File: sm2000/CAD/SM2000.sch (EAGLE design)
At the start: 361 parts, among them CN1 HDR100-3, CN10 ST-3509, CN11 HDR100-3, CN2 JS-MU3-002, CN3 DS-0518, CN5 ST-3509, CN8 ST-3509, J1 JMP-2PIN, J2 JMP-2PIN, J3 JMP-2PIN, J4 CONN-BOOM-XH-2A, P10 TPAD50, P11 TPAD50, P12 TPAD50, P13 TPAD50, P14 TPAD50, P16 TPAD50, P18 TPAD50, P19 TPAD50, P20 TPAD50, P21 TPAD50, P3 TPAD50, P4 TPAD50, P5 TPAD50, P6 TPAD50, P7 TPAD50, P8 TPAD50, P9 TPAD50, Q1 MMBT3904, Q10 MMBT3904, Q11 STR2P3LLH6, Q12 BRF92, Q13 BFQ19, Q14 RD01MUS2, Q15 MMBT3904, Q17 MMBT3904, Q18 MMBT3904, Q2 MMBT3904, Q3 MMBT3904, Q4 MMBT3904, Q5 MMBT3904, Q6 MMBT3904, Q7 BC548, Q8 BC549, Q9 STR2P3LLH6, SW1 SW-LC2259, SW2 TS-026, SW3 SW-LC2259EENP, SW4 TS-026, SW5 TS-02B, U1 STM32F405VGT6, U10 DNL, U11 L78MXX, U12 PGA-103+, U13 ADE-1, U14 SI570, U15 SI5351A, U2 L78MXX, U3 STMPS2141, U4 EMIF02-USB03F2, U5 L78MXX, U6 LD3985M33R, U7 SA612A, U8 LM386M-1, U9 LMV341, X1 BU-SMA-H, X2 BU-SMA-H

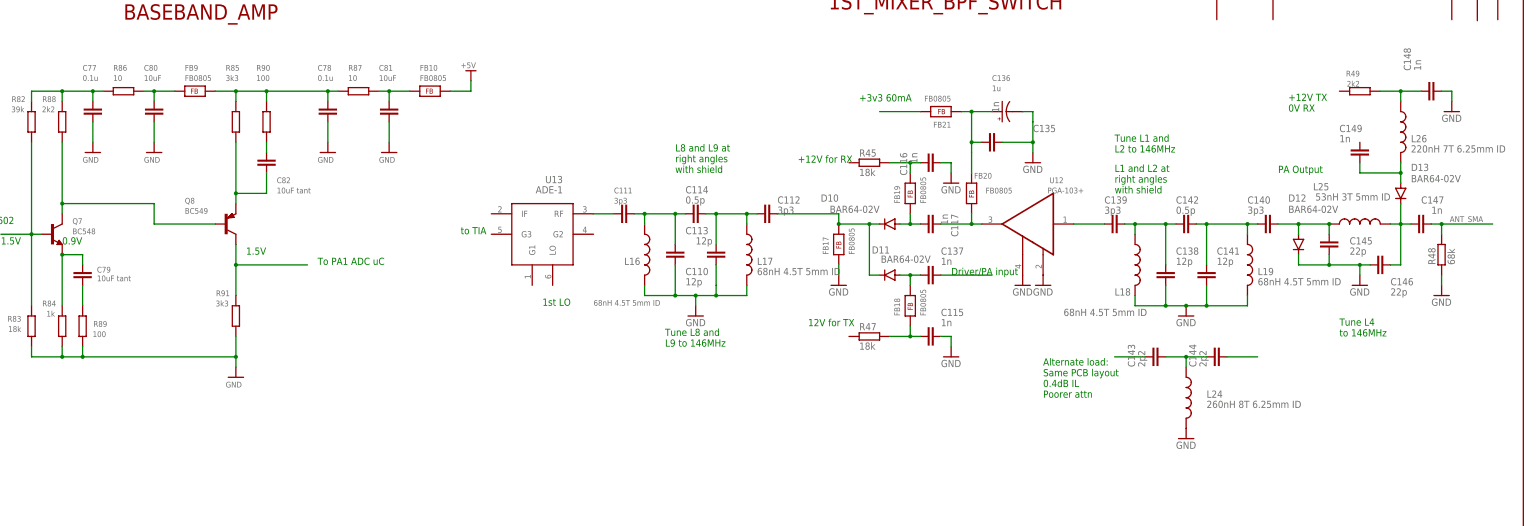
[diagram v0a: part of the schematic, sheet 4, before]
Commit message: 
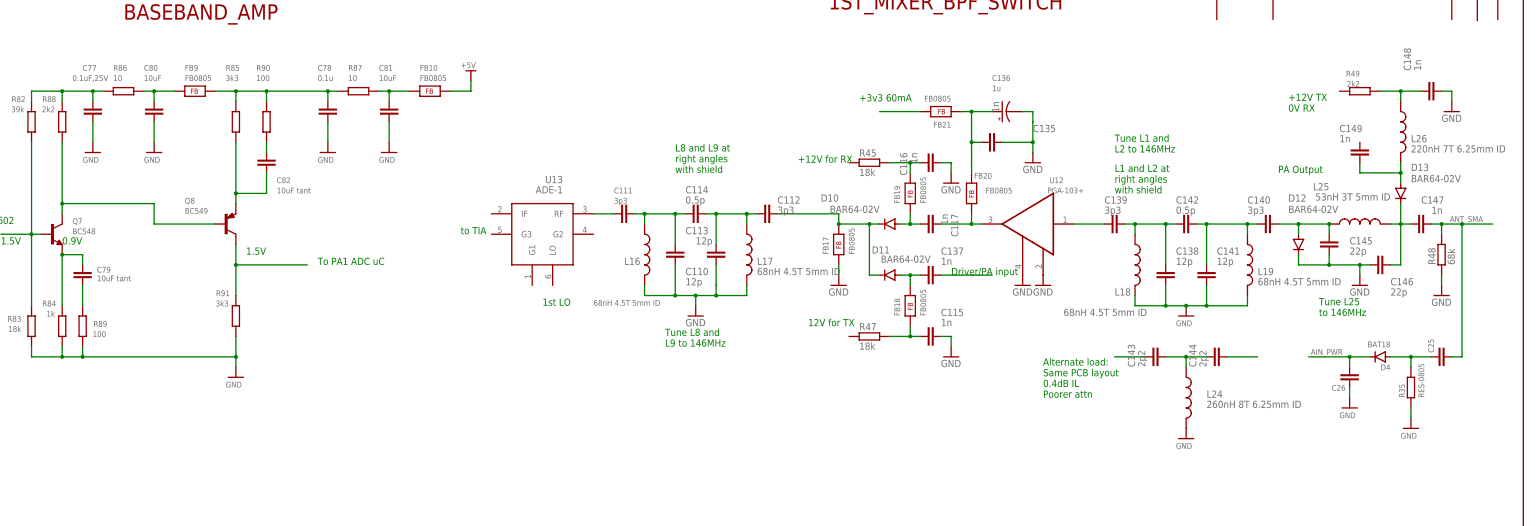
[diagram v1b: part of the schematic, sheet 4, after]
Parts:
- added C25, C26: (no value), _RoweTel:CAP-0805
- added D4: BAT18, _RoweTel:BAT18
- added R35: RES-0805, _RoweTel:RES-0805
- C77: value 0.1u -> 0.1uF,25V
- Q7: device transistor:-NPN-SOT23-EBC -> _RoweTel:MMBT3904
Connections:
- new net AIN_PWR: C26.2, D4.K
- new net N$57: C25.1, D4.A, R35.2
- net ANT_SMA: now also C25.2
- net GND: now also C26.1, R35.1
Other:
- note added: "Tune L25 to 146MHz"
- note removed: "Tune L4 to 146MHz"
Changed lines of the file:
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@@
 <layer number="101" name="Gehäuse" color="13" fill="1" visible="no" active="yes"/>
 <layer number="102" name="Mittellin" color="7" fill="1" visible="no" active="yes"/>
+<layer number="103" name="fp3" color="7" fill="1" visible="no" active="yes"/>
+<layer number="104" name="Name" color="7" fill="1" visible="no" active="yes"/>
 <layer number="105" name="Beschreib" color="9" fill="1" visible="no" active="no"/>
 <layer number="106" name="BGA-Top" color="4" fill="1" visible="no" active="no"/>
 <layer number="107" name="BD-Top" color="5" fill="1" visible="no" active="no"/>
+<layer number="108" name="fp8" color="7" fill="1" visible="no" active="yes"/>
+<layer number="109" name="fp9" color="7" fill="1" visible="no" active="yes"/>
+<layer number="110" name="fp0" color="7" fill="1" visible="no" active="yes"/>
+<layer number="111" name="KASTMAAT1" color="7" fill="1" visible="no" active="yes"/>
+<layer number="112" name="KASTMAAT2" color="7" fill="1" visible="no" active="yes"/>
+<layer number="113" name="FRNTTEKEN" color="7" fill="1" visible="no" active="yes"/>
+<layer number="114" name="FRNTMAAT1" color="7" fill="1" visible="no" active="yes"/>
+<layer number="115" name="FRNTMAAT2" color="7" fill="1" visible="no" active="yes"/>
+<layer number="116" name="Patch_BOT" color="7" fill="1" visible="no" active="yes"/>
+<layer number="117" name="BACKMAAT1" color="7" fill="1" visible="no" active="yes"/>
+<layer number="118" name="BACKMAAT2" color="7" fill="1" visible="no" active="yes"/>
+<layer number="119" name="KAP_TEKEN" color="7" fill="1" visible="no" active="yes"/>
+<layer number="120" name="KAP_MAAT1" color="7" fill="1" visible="no" active="yes"/>
+<layer number="121" name="tTestdril" color="7" fill="1" visible="no" active="yes"/>
+<layer number="122" name="bTestdril" color="7" fill="1" visible="no" active="yes"/>
+<layer number="123" name="tTestmark" color="7" fill="1" visible="no" active="yes"/>
+<layer number="124" name="bTestmark" color="7" fill="1" visible="no" active="yes"/>
+<layer number="125" name="BIFRNTTEK" color="7" fill="1" visible="no" active="yes"/>
+<layer number="126" name="BIFRNTMAT" color="7" fill="1" visible="no" active="yes"/>
+<layer number="130" name="SMDSTROOK" color="7" fill="1" visible="no" active="yes"/>
+<layer number="131" name="tAdjust" color="7" fill="1" visible="no" active="yes"/>
+<layer number="132" name="bAdjust" color="7" fill="1" visible="no" active="yes"/>
+<layer number="144" name="Drill_legend" color="7" fill="1" visible="no" active="yes"/>
+<layer number="151" name="HeatSink" color="7" fill="1" visible="no" active="yes"/>
+<layer number="199" name="Contour" color="7" fill="1" visible="no" active="yes"/>
 <layer number="200" name="200bmp" color="1" fill="10" visible="no" active="no"/>
+<layer number="201" name="Construction" color="7" fill="1" visible="no" active="yes"/>
+<layer number="202" name="TDIM" color="7" fill="1" visible="no" active="yes"/>
+<layer number="203" name="BDIM" color="7" fill="1" visible="no" active="yes"/>
+<layer number="204" name="BRD-DIM" color="7" fill="1" visible="no" active="yes"/>
+<layer number="205" name="SECTION-OTL" color="7" fill="1" visible="no" active="yes"/>
+<layer number="206" name="206bmp" color="7" fill="1" visible="no" active="yes"/>
+<layer number="207" name="207bmp" color="7" fill="1" visible="no" active="yes"/>
+<layer number="208" name="208bmp" color="7" fill="1" visible="no" active="yes"/>
+<layer number="209" name="209bmp" color="7" fill="1" visible="no" active="yes"/>
+<layer number="210" name="210bmp" color="7" fill="1" visible="no" active="yes"/>
+<layer number="216" name="BottomExtra" color="7" fill="1" visible="no" active="yes"/>
 <layer number="250" name="Descript" color="3" fill="1" visible="no" active="no"/>
 <layer number="251" name="SMDround" color="12" fill="11" visible="no" active="no"/>
+<layer number="254" name="OrgLBR" color="7" fill="1" visible="no" active="yes"/>
+<layer number="255" name="Accent" color="7" fill="1" visible="no" active="yes"/>
 </layers>
 <schematic xreflabel="%F%N/%S.%C%R" xrefpart="/%S.%C%R">
@@
 <part name="V161" library="A-SUPPLY2" deviceset="GND" device=""/>
 <part name="V162" library="A-SUPPLY2" deviceset="GND" device=""/>
-<part name="Q7" library="transistor" deviceset="*-NPN-" device="SOT23-EBC" value="BC548"/>
+<part name="Q7" library="_RoweTel" deviceset="MMBT3904" device="" value="BC548"/>
 <part name="R82" library="_RoweTel" deviceset="RES-0805" device="" value="39k"/>
 <part name="R83" library="_RoweTel" deviceset="RES-0805" device="" value="18k"/>
@@
 <part name="R85" library="_RoweTel" deviceset="RES-0805" device="" value="3k3"/>
 <part name="R86" library="_RoweTel" deviceset="RES-0805" device="" value="10"/>
-<part name="C77" library="_RoweTel" deviceset="CAP-0805" device="" value="0.1u"/>
+<part name="C77" library="_RoweTel" deviceset="CAP-0805" device="" value="0.1uF,25V"/>
 <part name="C78" library="_RoweTel" deviceset="CAP-0805" device="" value="0.1u"/>
 <part name="R87" library="_RoweTel" deviceset="RES-0805" device="" value="10"/>
@@
 <part name="U14" library="_RoweTel" deviceset="SI570" device=""/>
 <part name="U$7" library="A-SUPPLY2" deviceset="+3.3V" device=""/>
+<part name="D4" library="_RoweTel" deviceset="BAT18" device=""/>
+<part name="R35" library="_RoweTel" deviceset="RES-0805" device=""/>
+<part name="C25" library="_RoweTel" deviceset="CAP-0805" device=""/>
+<part name="C26" library="_RoweTel" deviceset="CAP-0805" device=""/>
+<part name="GND18" library="supply1" deviceset="GND" device=""/>
+<part name="GND19" library="supply1" deviceset="GND" device=""/>
 </parts>
 <sheets>
@@
 right angles
 with shield</text>
-<text x="386.08" y="185.42" size="1.778" layer="91">Tune L4
+<text x="381" y="190.5" size="1.778" layer="91">Tune L25
 to 146MHz</text>
 <text x="259.08" y="266.7" size="3.81" layer="94" ratio="10">1ST_MIXER_BPF_SWITCH</text>
@@
 <instance part="C77" gate="G$1" x="76.2" y="241.3" smashed="yes">
 <attribute name="NAME" x="73.66" y="251.46" size="1.4224" layer="95"/>
-<attribute name="VALUE" x="73.66" y="248.92" size="1.4224" layer="96"/>
+<attribute name="VALUE" x="71.12" y="248.92" size="1.4224" layer="96"/>
 </instance>
 <instance part="C78" gate="G$1" x="134.62" y="241.3" smashed="yes">
@@
 </instance>
 <instance part="GND45" gate="1" x="347.98" y="190.5" smashed="yes">
-<attribute name="VALUE" x="345.44" y="187.96" size="1.778" layer="96"/>
+<attribute name="VALUE" x="345.44" y="187.96" size="1.4224" layer="96"/>
 </instance>
 <instance part="L24" gate="G$1" x="347.98" y="170.18" smashed="yes">
@@
 </instance>
 <instance part="GND46" gate="1" x="347.98" y="160.02" smashed="yes">
-<attribute name="VALUE" x="345.44" y="157.48" size="1.778" layer="96"/>
+<attribute name="VALUE" x="345.44" y="157.48" size="1.4224" layer="96"/>
 </instance>
 <instance part="D12" gate="G$1" x="375.92" y="208.28" smashed="yes" rot="R270">
@@
 <attribute name="VALUE" x="162.56" y="122.555" size="1.4224" layer="96" ratio="9"/>
 </instance>
+<instance part="D4" gate="G$1" x="396.24" y="180.34" rot="R180"/>
+<instance part="R35" gate="G$1" x="403.86" y="172.72" rot="R90"/>
+<instance part="C25" gate="G$1" x="411.48" y="180.34" rot="R90"/>
+<instance part="C26" gate="G$1" x="388.62" y="175.26" rot="R180"/>
+<instance part="GND18" gate="1" x="388.62" y="167.64" smashed="yes">
+<attribute name="VALUE" x="386.08" y="165.1" size="1.4224" layer="96"/>
+</instance>
+<instance part="GND19" gate="1" x="403.86" y="162.56" smashed="yes">
+<attribute name="VALUE" x="401.32" y="160.02" size="1.4224" layer="96"/>
+</instance>
 </instances>
 <busses>
@@
 <junction x="391.16" y="203.2"/>
 </segment>
+<segment>
+<pinref part="C26" gate="G$1" pin="1"/>
+<wire x1="388.62" y1="172.72" x2="388.62" y2="170.18" width="0.1524" layer="91"/>
+<pinref part="GND18" gate="1" pin="GND"/>
+</segment>
+<segment>
+<pinref part="R35" gate="G$1" pin="1"/>
+<wire x1="403.86" y1="167.64" x2="403.86" y2="165.1" width="0.1524" layer="91"/>
+<pinref part="GND19" gate="1" pin="GND"/>
+</segment>
 </net>
 <net name="N$103" class="0">
@@
 <wire x1="408.94" y1="213.36" x2="411.48" y2="213.36" width="0.1524" layer="91"/>
 <pinref part="R48" gate="G$1" pin="2"/>
-<wire x1="411.48" y1="213.36" x2="424.18" y2="213.36" width="0.1524" layer="91"/>
+<wire x1="411.48" y1="213.36" x2="416.56" y2="213.36" width="0.1524" layer="91"/>
+<wire x1="416.56" y1="213.36" x2="424.18" y2="213.36" width="0.1524" layer="91"/>
 <wire x1="411.48" y1="210.82" x2="411.48" y2="213.36" width="0.1524" layer="91"/>
 <junction x="411.48" y="213.36"/>
 <label x="413.512" y="213.868" size="1.4224" layer="95" ratio="10"/>
+<wire x1="416.56" y1="213.36" x2="416.56" y2="180.34" width="0.1524" layer="91"/>
+<pinref part="C25" gate="G$1" pin="2"/>
+<wire x1="416.56" y1="180.34" x2="414.02" y2="180.34" width="0.1524" layer="91"/>
+<junction x="416.56" y="213.36"/>
 </segment>
 </net>
@@
 </segment>
 </net>
+<net name="N$57" class="0">
+<segment>
+<pinref part="C25" gate="G$1" pin="1"/>
+<pinref part="D4" gate="G$1" pin="A"/>
+<wire x1="408.94" y1="180.34" x2="403.86" y2="180.34" width="0.1524" layer="91"/>
+<pinref part="R35" gate="G$1" pin="2"/>
+<wire x1="403.86" y1="180.34" x2="398.78" y2="180.34" width="0.1524" layer="91"/>
+<wire x1="403.86" y1="177.8" x2="403.86" y2="180.34" width="0.1524" layer="91"/>
+<junction x="403.86" y="180.34"/>
+</segment>
+</net>
+<net name="AIN_PWR" class="0">
+<segment>
+<pinref part="D4" gate="G$1" pin="K"/>
+<pinref part="C26" gate="G$1" pin="2"/>
+<wire x1="393.7" y1="180.34" x2="388.62" y2="180.34" width="0.1524" layer="91"/>
+<wire x1="388.62" y1="180.34" x2="388.62" y2="177.8" width="0.1524" layer="91"/>
+<wire x1="388.62" y1="180.34" x2="378.46" y2="180.34" width="0.1524" layer="91"/>
+<junction x="388.62" y="180.34"/>
+<label x="378.968" y="180.848" size="1.4224" layer="95" ratio="10"/>
+</segment>
+</net>

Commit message: Intermediate update: Fix resistor tolerances fix cap working voltages Fix some library items for no name & no value email Schematic Updates 01/01/2016 item 1. email Commits to SVN 01/02/2016 items 1, i,ii,iii,iv, 2,3,4 RGB
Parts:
- removed C36, C47: 1uF,16V, _RoweTel:CAP-0805
- removed C38: 10nF,25V, _RoweTel:CAP-0805
- removed C41, C45: 100nF,25V, _RoweTel:CAP-0805
- removed LED6: DNL, _RoweTel:SML-LX0603SRW
- removed R23: 0 Ohm, _RoweTel:RES-0805
- removed R9: DNL, _RoweTel:RES-0805
- removed U6: LD3985M33R, _RoweTel:LD3985
- removed X1, X2: BU-SMA-H, _RoweTel:BU-SMA-H
- C100, C93: value 33p -> 33pF,50V
- C110: value 12p -> 12pF.50V
- C111, C112, C139, C140: value 3p3 -> 3.3pF,50V
- C113, C138, C141: value 12p -> 12pF,50V
- C114, C142: value 0.5p -> 0.5pF,50V
- C115, C116, C117, C130, C133, C134, C135, C137, C147, C148, C149, C88, C90, C96, C98: value 1n -> 1nF,25V
- C118, C121, C124, C125, C126, C131, C78: value 0.1u -> 0.1uF,25V
- C120: value 39pF -> 39pF,50V
- C122, C89: value 5p6 -> 5.6pF,50V
- C127: value 27pF -> 27pF,50V
- C128, C132: value 150pF -> 150pF,50V
- C129, C91, C92, C97: value 0.1u -> 0.1uF.25V
- C136: value 1u -> 1uF,25V
- C143, C144: value 2p2 -> 2.2pF,50V
- C145, C94: value 22p -> 22pF,50V
- C146: value 22p -> 22pF,25V
- C25: value (none) -> 1pF,50V
- C26: value (none) -> 1nF,25V
- C28: value 100nF -> 100nF,25V
- C87: value 22pF -> 22pF,50V
- C95: value 1n DNL -> 1nF,25V
- C99: value 47p -> 47pF,50V
- L14, L15: value 57nH air core 4T 2mm ID -> 57nH
- L16, L17, L18, L19: value 68nH 4.5T 5mm ID -> 68nH
- L24: value 260nH 8T 6.25mm ID -> 260nH
- L26: value 220nH 7T 6.25mm ID -> 220nH
- Q7: value BC548 -> MMBT3904
- Q8: value BC549 -> MMBT3906
- R101, R104, R115, R92: value 150 -> 150,1%
- R102, R103, R109, R113, R84, R94: value 1k -> 1K,1%
- R105, R106, R107: value 0R -> 0 Ohm
- R108, R60, R93: value 3k -> 3K,1%
- R110, R70, R80, R86, R87, R96, R97: value 10 -> 10,1%
- R111: value 33k -> 33K,1%
- R112: value 15k -> 15K,1%
- R114: value 50 -> 50,1%
- R35: value RES-0805 -> 330,1%
- R45, R47, R83: value 18k -> 18K,1%
- R48: value 68k -> 68K,1%
- R49, R88: value 2k2 -> 2.2K,1%
- R55: value 10k -> 10K,1%
- R59, R72: value 330 -> 330,1%
- R63, R73: value 680 -> 680,1%
- R64, R74: value 10K -> 10K,1%
- R65, R68, R75, R78: value 2.2K -> 2.2K,1%
- R66, R76: value 180 -> 180,1%
- R67, R77: value 15 -> 15,1%
- R69, R79: value 470 -> 470,1%
- R71, R81: value 47 -> 47,1%
- R82: value 39k -> 39K,1%
- R85, R91: value 3k3 -> 3.3K,1%
- R89, R90: value 100 -> 100,1%
- R95: value 50 -> 49.4,1%
- R98: value 47 DNL -> 47,1%, DNL
- R99: value 4k7 -> 4.7K,1%
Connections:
- net N$38 renamed DRIVER/PA_INPUT
- removed net N$100: C71.2, C75.1, X1.1
- removed net N$37 (its old number): C38.1, U6.BYBASS
- removed net N$40: Q11.D, R80.1
- removed net N$52: LED6.A, R9.1
- removed net N$56: L20.1
- removed net N$79: L11.2, L13.2, R97.1
- removed net N$90: C69.1, C76.2, X2.1
- new net N$19: L13.1, R97.1
- new net PA_OUTPUT: C149.2
- new net RX+12V: Q9.D, R70.2
- new net TIAIN: C71.2, C75.1, U13.G3
- new net TIAOUT: C69.1, C76.2, L20.1
- new net TX+12V: L11.2, Q11.D, R47.1, R49.2, R80.1
- net +12V: no longer Q11.S, Q9.S, R17.2, R33.2
- net +12V_RX: now also R45.1; no longer Q9.D, R70.2
- net +3.3V: no longer C36.1, C41.1, R23.1, R9.2, U6.VOUT
- net +5V: no longer C45.1, C47.1, U6.INH, U6.VIN
- net +9V: now also L13.2; no longer L13.1
- net +VIN: now also Q11.S, Q9.S, R17.2, R33.2
- net GND: no longer C36.2, C38.2, C41.2, C45.2, C47.2, LED6.C, U6.GND, X1.2, X2.2
- net VDD: no longer R23.2
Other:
- note added: "ADC3"
- note added: "L10 6T 6.25mm"
- note added: "L12 3T 6.25mm"
- note added: "L14 57nH, Air Core, 4T, 2mm ID"
- note added: "L15 57nH, Air Core, 4T, 2mm ID"
- note added: "L16 68nH,4.5T 5mm ID"
- note added: "L17 68nH,4.5T 5mm ID"
- note added: "L18 68nH,4.5T 5mm ID"
- note added: "L19 68nH,4.5T 5mm ID"
- note added: "L24 260nH 8T 6.25mm ID"
- note added: "L25 53nH,3T 5mm ID"
- note added: "L26 220nH,7T 6.25mm ID"
- note added: "L9 3T 6.25mm"
- note added: "TERMINATION INSENSiTIVE AMPLIFIEER"
- note removed: "+12V TX 0V RX"
- note removed: "+12V for RX"
- note removed: "1K,1%"
- note removed: "5.0V -> 3.3V PS"
- note removed: "6T 6.25mm"
- note removed: "Driver/PA input"
- note removed: "From TIA"
- note removed: "PA Output"
- note removed: "SML-LX0603SRW-TR"
- note removed: "TERMINATION INSENSATIVE AMPLIFIEER"
- moved on the sheet: C100, C110, C111, C112, C113, C114, C138, C139, C140, C141, C149, C77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

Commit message: Update schematic. Moved new component footprints onto PCB Matched schematic to emailchange lists. reorganized circuitry blocks on pages. RGB
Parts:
- added C27: 1nF,25V, _RoweTel:CAP-0805
- added J10, J11, J12, J5, J6, J7, J8, J9: JMPR-2X2, _RoweTel:JMPR-2X2
- added SH4, SH5: SHUNT, _RoweTel:SHUNT
- C119, C80, C81: value 10uF -> 10uF,25V,EL; device _RoweTel:CAP-0805 -> _RoweTel:CAP-10UF-WJ5
- C79, C82: value 10uF tant -> 10uF,25V,EL; device _RoweTel:CAP-0805 -> _RoweTel:CAP-10UF-WJ5
- R114: value 50,1% -> 49.9,1%
- R95: value 49.4,1% -> 49.9,1%
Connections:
- net +12V_RX_ENB renamed +12VRXENB
- removed net N$127: C111.2, U13.RF
- new net N$40: C126.2, J6.1
- new net N$52: C100.1, J9.1, L14.2
- new net N$56: C111.2, J12.2
- new net N$58: J12.1, U13.RF
- new net N$59: C27.2, J10.1
- new net N$61: C27.1, U12.1N
- new net N$63: J8.1
- new net N$79: C112.1, J11.1
- new net TIA_OUT: C69.1, C76.2, J5.1, L20.1
- net ANT_SMA: now also J9.2; no longer C100.1, L14.2
- net BBAMP: now also J7.1
- net GND: now also J10.3, J10.4, J11.3, J11.4, J12.3, J12.4, J5.3, J5.4, J6.3, J6.4, J7.3, J7.4, J8.3, J8.4, J9.3, J9.4
- net N$104: now also J7.2
- net N$11: now also J10.2; no longer U12.1N
- net N$112: now also J8.2
- net N$135: now also J11.2; no longer C112.1
- net N$49: now also J6.2; no longer C126.2
- net TIAOUT: now also J5.2; no longer C69.1, C76.2, L20.1
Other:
- note added: "+12V RX PWR"
- note added: "+12V TX PWR"
- note added: "VDD -> AVDD"
- note removed: "VDD -> AVDD POWER SOURCE"
- moved on the sheet: C1, C100, C110, C111, C112, C113, C114, C115, C116, C117, C126, C135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

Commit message: Implemented changes from D. Rowes email: Comments #1 RGB
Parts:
- removed C64: 22uF,25V, _RoweTel:CAP-0805
- removed C66: 100nF,25V, _RoweTel:CAP-0805
- removed U5: L78MXX, _RoweTel:L78MXX
- added C101: 10nF,25V, _RoweTel:CAP-0805
- added C103, C164: 100nF,25V, _RoweTel:CAP-0805
- added C107: 100nF,25V, AA-ipc-7351-capacitor:CAPACITOR_0402
- added C108: 20pF,50V, AA-ipc-7351-capacitor:CAPACITOR_0402
- added C109: 8.2nF,25V, ipc-7351-capacitor:CAPACITOR_0603
- added C150, C179: 22uF,25V, _RoweTel:CAP-1210
- added C166: 470nF,25V, ipc-7351-capacitor:CAPACITOR_0603
- added C167: 22uF,25V,1210, AA-ipc-7351-capacitor:CAPACITOR_1210
- added C29, C31: CAP-10UF-WJ5, _RoweTel:CAP-10UF-WJ5
- added C36: 1nF,25V, _RoweTel:CAP-0805
- added J13: JMPR-2X2, _RoweTel:JMPR-2X2
- added L1: 4.2uH, _RoweTel:SRR5028
- added R127: 124.0K,1%, AA-ipc-7351-resistor:RESISTOR_0402
- added R128: 22.1K,1%, AA-ipc-7351-resistor:RESISTOR_0402
- added R129: 10K,1%, AA-ipc-7351-resistor:RESISTOR_0402
- added U17: TPS54329E, _RoweTel:TPS54329E
- added U6: LD3985M33R, _RoweTel:LD3985
- C1: value .33uF,25V -> 100nF,25V
- C5, C7: value .33uF,25V -> CAP-10UF-WJ5; device _RoweTel:CAP-0805 -> _RoweTel:CAP-10UF-WJ5
- C65: value 1uF,16V -> 1uF,25V
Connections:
- removed net N$63: J8.1
- new net N$127: C101.1, U6.BYBASS
- new net N$169: C107.1, U17.VBST
- new net N$170: C108.2, R127.2, R128.1, U17.VFB
- new net N$171: C109.1, U17.SS
- new net N$172: C166.1, U17.VREG5
- new net N$173: R129.2, U17.EN
- new net N$222: C150.1, C164.1, C179.1, C36.1, R129.1, R21.2, U17.VIN
- new net N$90: J13.2, U13.G3
- new net SW: C107.2, L1.1, U17.SW
- net +3.3V: now also C8.1, U11.OUT
- net +5V: now also C108.1, C167.1, C7.1, FB8.1, L1.2, R127.1, U11.IN; no longer C6.1, U5.OUT
- net +9V: now also L11.2; no longer L13.2
- net +VIN: now also C31.1, U2.IN
- net AVDD: now also C5.1, C6.1, FB7.1, U6.VOUT; no longer C64.1, C66.1, FB8.2
- net GND: now also C101.2, C103.2, C109.2, C150.2, C164.2, C166.2, C167.2, C179.2, C29.2, C31.2, C36.2, J13.3, J13.4, R128.2, U17.EP, U17.GND, U6.GND; no longer C64.2, C66.2, U5.GND
- net N$144: now also XTAL3.2; no longer XTAL3.1
- net N$145: now also XTAL3.1; no longer XTAL3.2
- net N$54: now also C103.1, C29.1, FB8.2, U6.INH, U6.VIN; no longer C5.1, C7.1, R21.2, U11.IN, U2.IN, U5.IN
- net TIAIN: now also J13.1; no longer U13.G3
- net TX+12V: now also L13.2; no longer L11.2
- net VDD: no longer C8.1, FB7.1, FB8.1, U11.OUT
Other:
- note added: "12 - 15VDC -> 5.0VDC"
- note added: "5.0V -> 3.3V PS"
- note added: "LOCAL OSCILLATOR"
- note added: "Notes"
- note added: "TERMINATION INSENSITIVE AMPLIFIER"
- note added: "Vin -> 9V"
- note removed: "LOCAL OSCILATOR"
- note removed: "TERMINATION INSENSiTIVE AMPLIFIEER"
- note removed: "to TIA"
